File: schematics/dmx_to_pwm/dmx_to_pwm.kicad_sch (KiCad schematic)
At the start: 27 parts, among them J1 DMX-IN, Q1 BS170, Q10 BS170, Q11 BS170, Q12 BS170, Q2 BS170, Q3 BS170, Q4 BS170, Q5 BS170, Q6 BS170, Q7 BS170, Q8 BS170, Q9 BS170, U1 SN75176AP

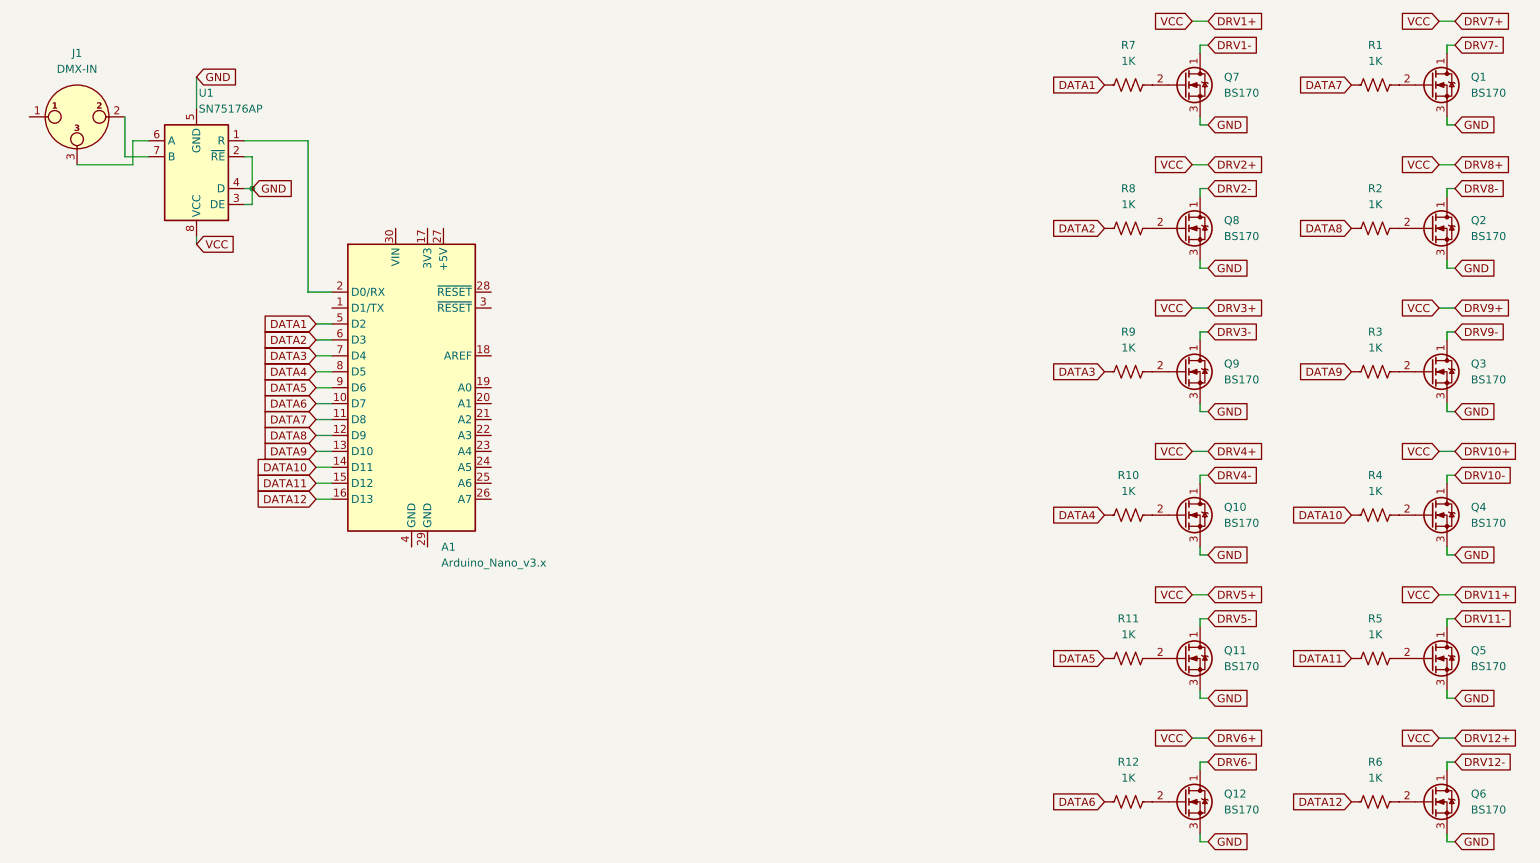
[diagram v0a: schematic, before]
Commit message: updated dmx-to-pwm schematics
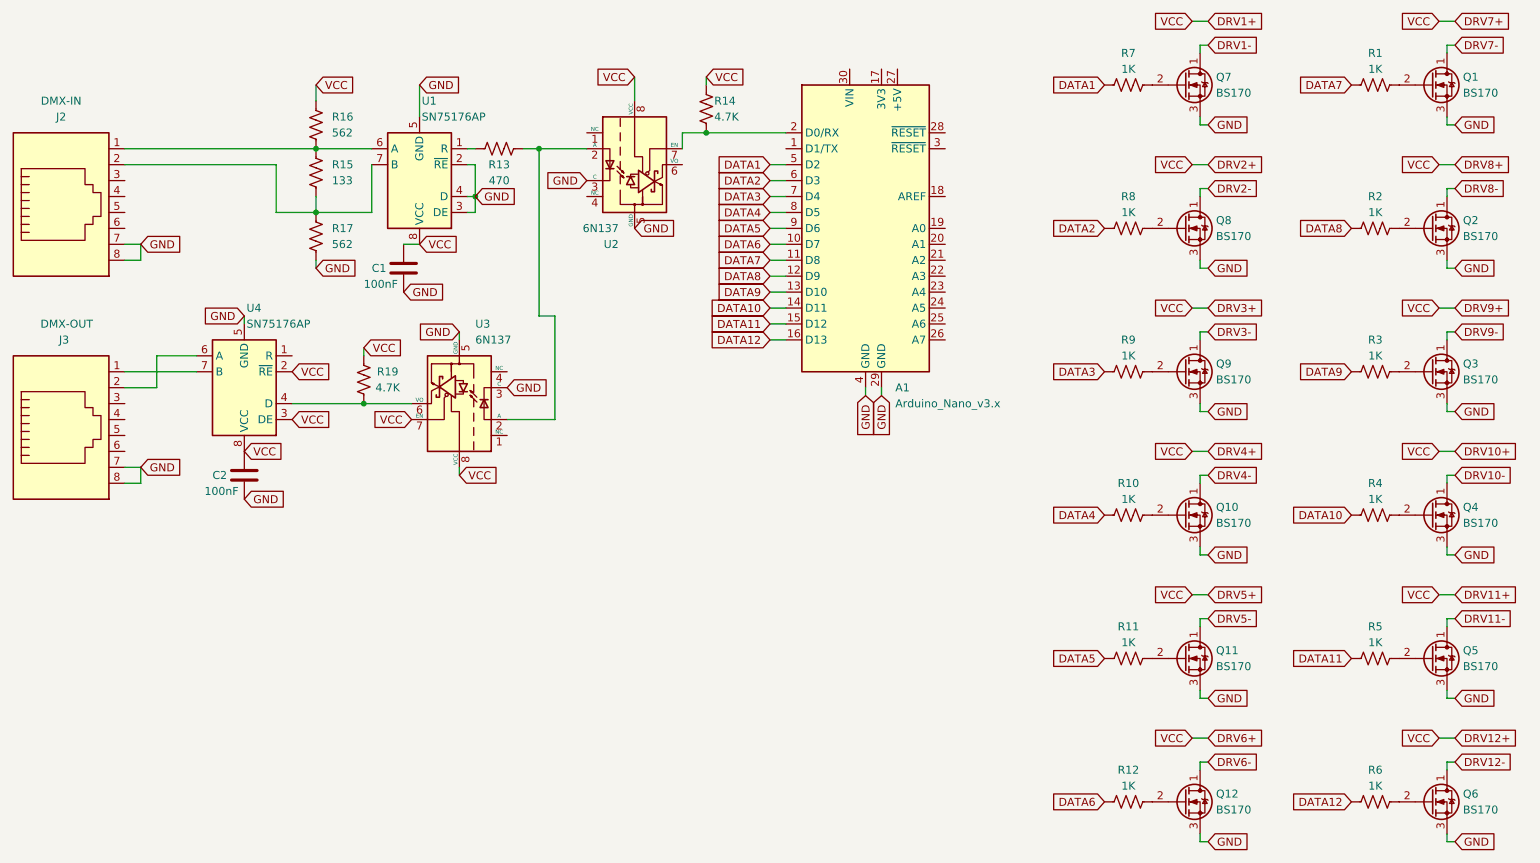
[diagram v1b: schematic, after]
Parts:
- removed J1: DMX-IN, symbol Connector_Audio:XLR3
- added C1, C2: 100nF, symbol Device:C
- added J2: DMX-IN, symbol Connector:RJ45
- added J3: DMX-OUT, symbol Connector:RJ45
- added R13: 470, symbol Device:R_US
- added R14, R19: 4.7K, symbol Device:R_US
- added R15: 133, symbol Device:R_US
- added R16, R17: 562, symbol Device:R_US
- added U2, U3: 6N137, Package_DIP:DIP-8_W7.62mm, symbol Isolator:6N137
- added U4: SN75176AP, Package_DIP:DIP-8_W7.62mm, symbol Interface_UART:SN75176AP
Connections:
- net DRV1+: now also C1.1, C2.1, R14.1, R16.1, R19.2, U2.8 (VCC), U3.7 (EN), U3.8 (VCC), U4.2 (~{RE}), U4.3 (DE), U4.8 (VCC)
- net GND: now also A1.29 (GND), A1.4 (GND), C1.2, C2.2, J2.7, J2.8, J3.7, J3.8, R17.2, U2.3 (C), U2.5 (GND), U3.3 (C), U3.5 (GND), U4.5 (GND)
- net at U1.1 (R): now also R13.1; no longer A1.2 (D0/RX)
- net at U1.6 (A): now also J2.1, R15.1, R16.2
- net at U1.7 (B): now also J2.2, R15.2, R17.1
- new net: A1.2 (D0/RX), R14.2, U2.7 (EN)
- new net: R13.2, U2.2 (A), U3.2 (A)
- new net: J3.1, U4.7 (B)
- new net: J3.2, U4.6 (A)
- new net: R19.1, U3.6 (VO), U4.4 (D)
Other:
- moved on the sheet: A1, U1
